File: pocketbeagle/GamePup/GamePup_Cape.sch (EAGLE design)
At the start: 47 parts, among them T1 3904, T2 3904, U2 TPD4S012DRY, X2 USB_HOST, X4 SPI-LCD-(1.8IN)

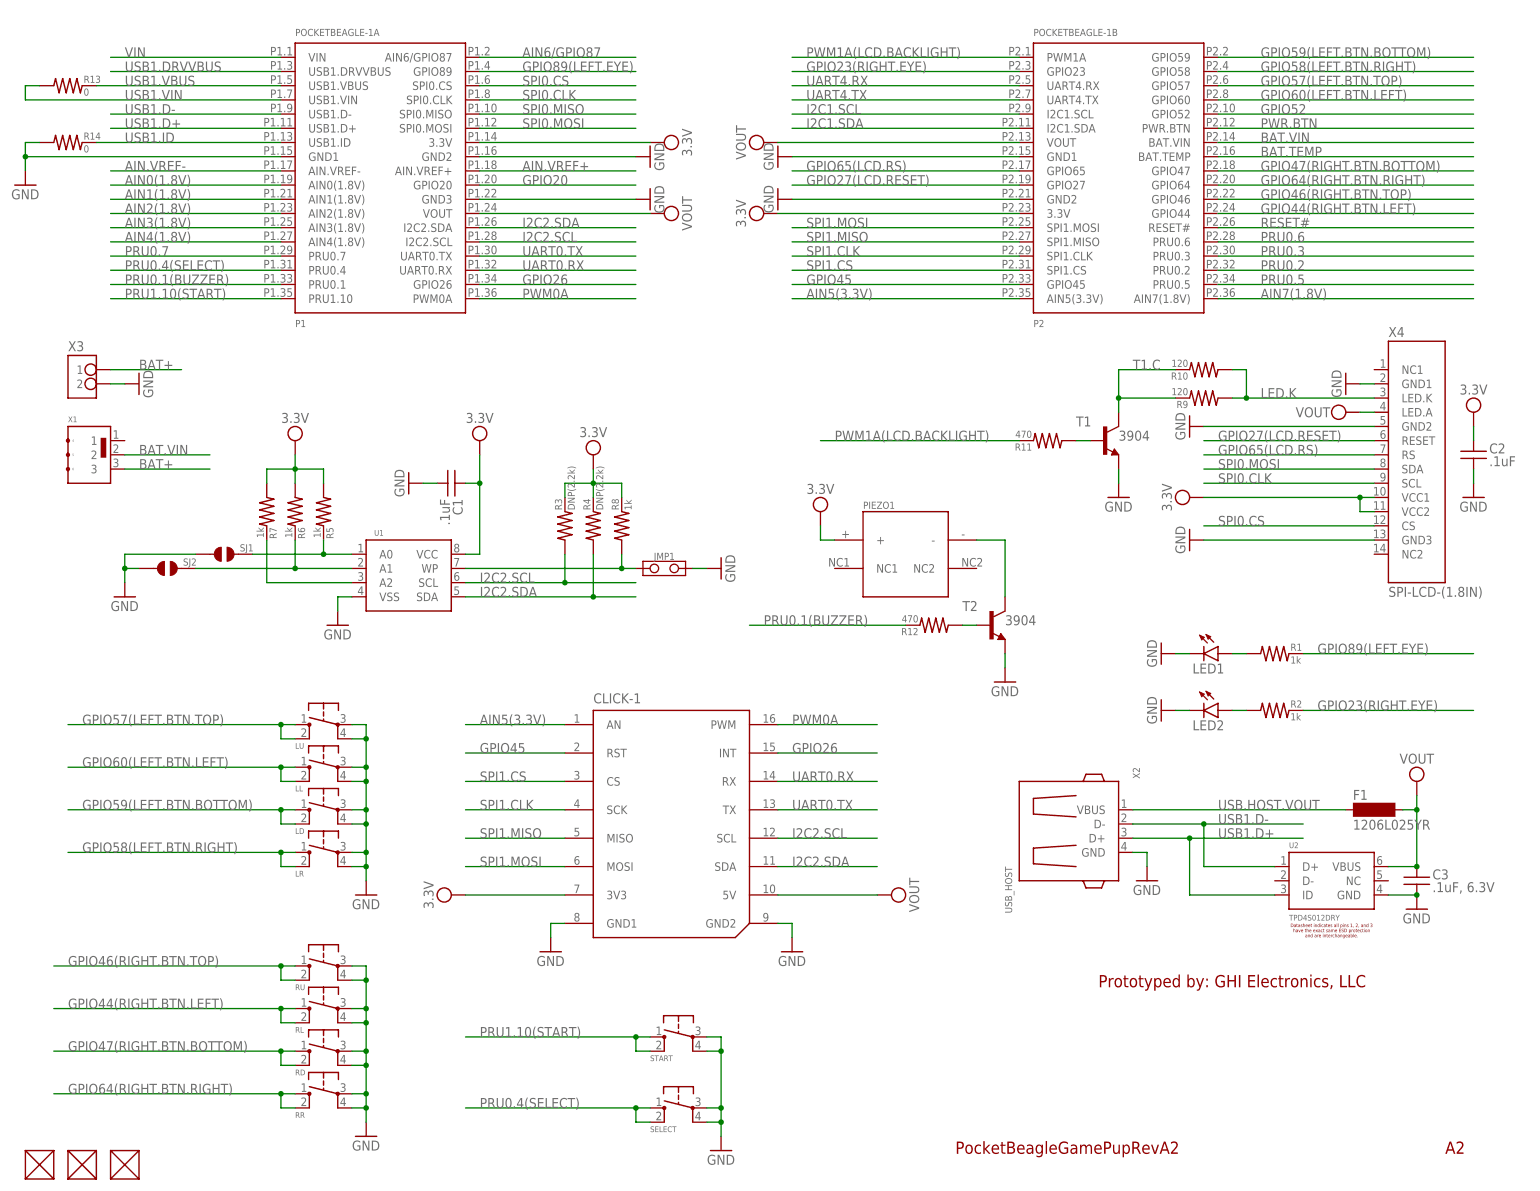
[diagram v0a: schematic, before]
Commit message: GamePup: update to A4
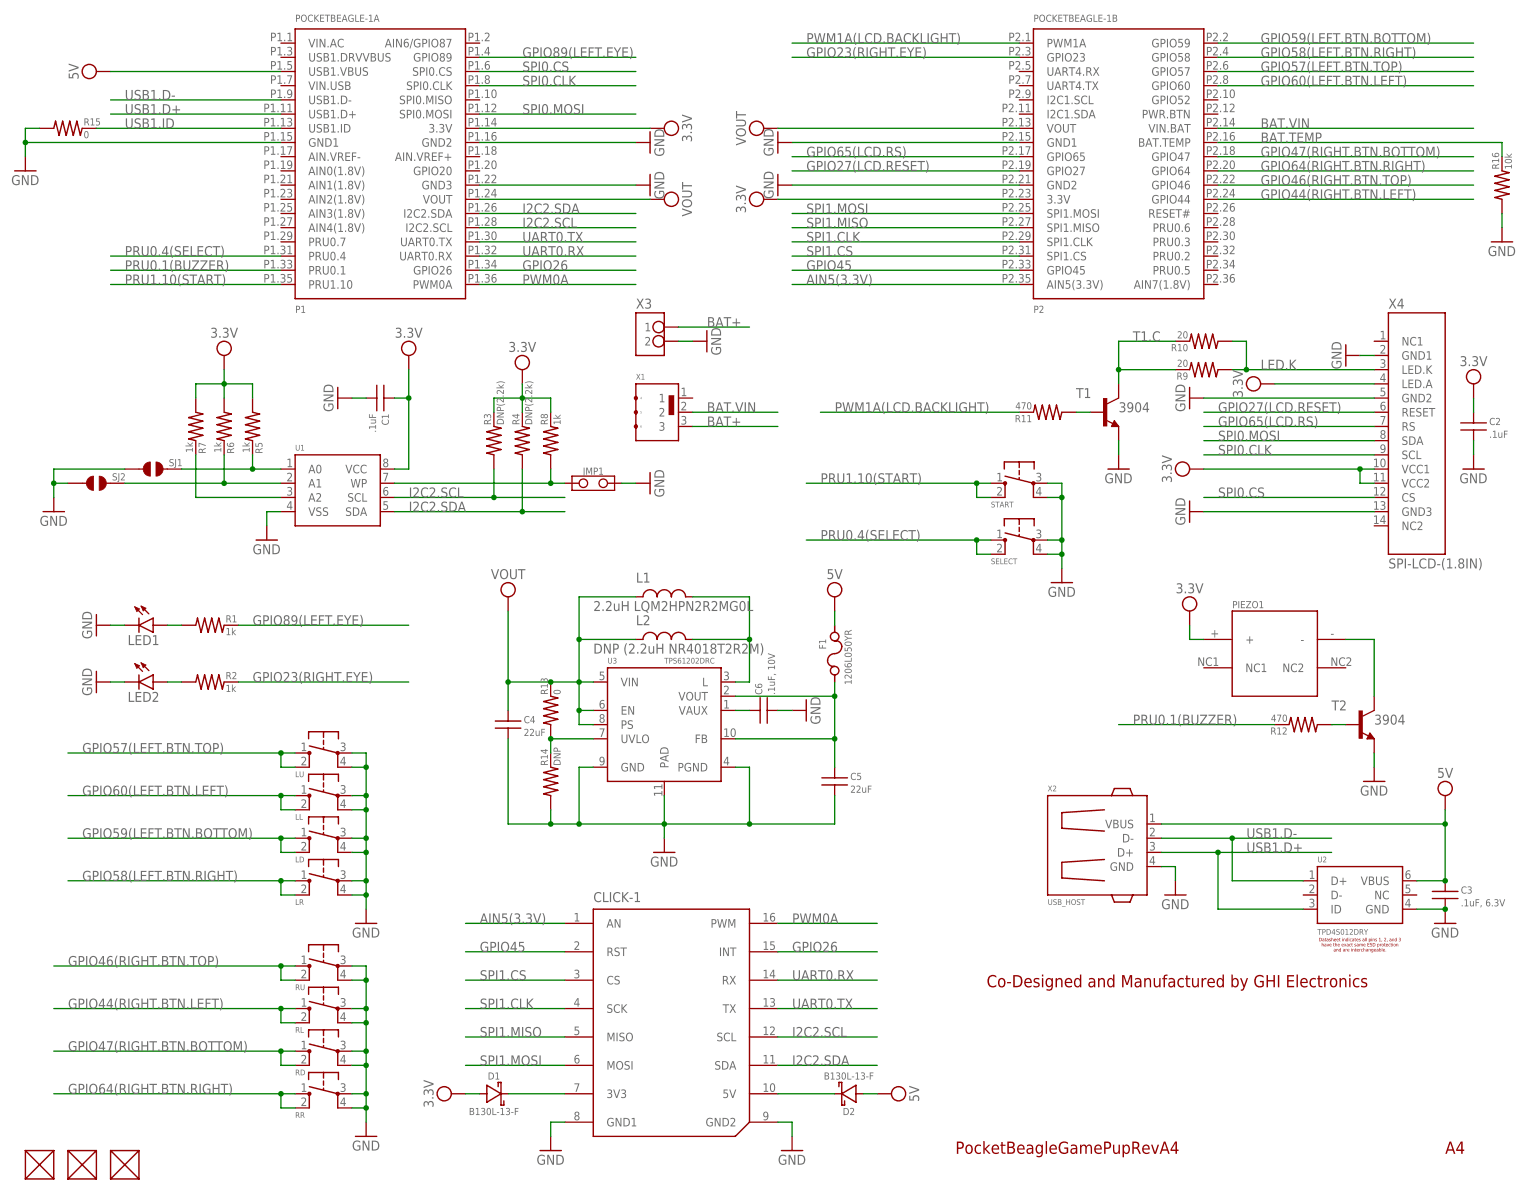
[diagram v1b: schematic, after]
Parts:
- added C4, C5: 22uF, GHI-BasicComponents:CAPACITOR-(INCH)-0805
- added C6: .1uF, 10V, GHI-BasicComponents:CAPACITOR-(INCH)-0402
- added D1, D2: B130L-13-F, GHI-BasicComponents:DIODE-SCHOTTKY-(DIODES)-SMA
- added L1: 2.2uH LQM2HPN2R2MG0L, GHI-BasicComponents:INDUCTOR-(INCH)-1008
- added L2: DNP (2.2uH NR4018T2R2M), GHI-BasicComponents:INDUCTOR-(TAIYO-YUDEN)-NRS40
- added R15: 0, GHI-BasicComponents:RESISTOR-(INCH)-0402
- added R16: 10k, GHI-BasicComponents:RESISTOR-(INCH)-0402
- added U3: TPS61202DRC, GHI-IC:TPS6120X
- F1: value 1206L025YR -> 1206L050YR; device inductor-neosid:SM-1206 -> GHI-BasicComponents:FUSE-(INCH)-1206
- POCKETBEAGLE-1: value POCKETBEAGLE-(ORIGIN-CENTER) -> POCKETBEAGLE-(ORIGIN-CENTER)-SMT.PADS(ONLY)-NO.RESTRICT; device GHI-Solutions:POCKETBEAGLE-(ORIGIN-CENTER) -> GHI-Solutions:POCKETBEAGLE-(ORIGIN-CENTER)-SMT.PADS(ONLY)-NO.RESTRICT
- R10, R9: value 120 -> 20
- R14: value 0 -> DNP
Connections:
- removed net AIN.VREF+: POCKETBEAGLE-1A.AIN.VREF+
- removed net AIN.VREF-: POCKETBEAGLE-1A.AIN.VREF-
- removed net AIN0(1.8V): POCKETBEAGLE-1A.AIN0(1.8V)
- removed net AIN1(1.8V): POCKETBEAGLE-1A.AIN1(1.8V)
- removed net AIN2(1.8V): POCKETBEAGLE-1A.AIN2(1.8V)
- removed net AIN3(1.8V): POCKETBEAGLE-1A.AIN3(1.8V)
- removed net AIN4(1.8V): POCKETBEAGLE-1A.AIN4(1.8V)
- removed net AIN6/GPIO87: POCKETBEAGLE-1A.AIN6/GPIO87
- removed net AIN7(1.8V): POCKETBEAGLE-1B.AIN7(1.8V)
- removed net GPIO20: POCKETBEAGLE-1A.GPIO20
- removed net GPIO52: POCKETBEAGLE-1B.GPIO52
- removed net I2C1.SCL: POCKETBEAGLE-1B.I2C1.SCL
- removed net I2C1.SDA: POCKETBEAGLE-1B.I2C1.SDA
- removed net PRU0.2: POCKETBEAGLE-1B.PRU0.2
- removed net PRU0.3: POCKETBEAGLE-1B.PRU0.3
- removed net PRU0.5: POCKETBEAGLE-1B.PRU0.5
- removed net PRU0.6: POCKETBEAGLE-1B.PRU0.6
- removed net PRU0.7: POCKETBEAGLE-1A.PRU0.7
- removed net PWR.BTN: POCKETBEAGLE-1B.PWR.BTN
- removed net RESET#: POCKETBEAGLE-1B.RESET#
- removed net SPI0.MISO: POCKETBEAGLE-1A.SPI0.MISO
- removed net UART4.RX: POCKETBEAGLE-1B.UART4.RX
- removed net UART4.TX: POCKETBEAGLE-1B.UART4.TX
- removed net USB.HOST.VOUT: F1.1, X2.VBUS
- removed net USB1.DRVVBUS: POCKETBEAGLE-1A.USB1.DRVVBUS
- removed net USB1.VBUS: POCKETBEAGLE-1A.USB1.VBUS, R13.2
- removed net USB1.VIN: POCKETBEAGLE-1A.USB1.VIN, R13.1
- removed net VIN: POCKETBEAGLE-1A.VIN
- new net 3.3V-PROTECTED: CLICK-1.3V3, D1.CATHODE
- new net 5V: C3.1, D2.ANODE, F1.2, POCKETBEAGLE-1A.USB1.VBUS, U2.VBUS, X2.VBUS
- new net 5V-PROTECTED: CLICK-1.5V, D2.CATHODE
- new net BOOST.5VOUT: C5.1, F1.1, U3.FB, U3.VOUT
- new net L: L1.2, L2.2, U3.L
- new net N$40: R13.1, R14.2, U3.UVLO
- new net VAUX: C6.1, U3.VAUX
- net 3.3V: now also D1.ANODE, X4.LED.A; no longer CLICK-1.3V3
- net BAT.TEMP: now also R16.2
- net BAT.VIN: now also POCKETBEAGLE-1B.VIN.BAT; no longer POCKETBEAGLE-1B.BAT.VIN
- net GND: now also C4.2, C5.2, C6.2, R15.1, R16.1, U3.GND, U3.PAD, U3.PGND
- net USB1.ID: now also R15.2; no longer R14.2
- net VOUT: now also C4.1, L1.1, L2.1, R13.2, U3.EN, U3.PS, U3.VIN; no longer C3.1, CLICK-1.5V, F1.2, U2.VBUS, X4.LED.A
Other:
- note added: "A4"
- note added: "Co-Designed and Manufactured by GHI Electronics"
- note added: "PocketBeagleGamePupRevA4"
- note removed: "A2"
- note removed: "PocketBeagleGamePupRevA2"
- note removed: "Prototyped by: GHI Electronics, LLC"
- moved on the sheet: C1, C2, C3, CLICK-1, JMP1, LD, LED1, LED2, LL, LR, LU, PIEZO1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
